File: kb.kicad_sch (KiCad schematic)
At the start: 191 parts, among them J1 Conn_02x04, J2 10029449-001RLF, J3 Conn_01x05, J4 Conn_01x10, J5 Conn_01x07, J6 Conn_01x06, SW1 RotaryEncoder_Switch, U1 Pico, U2 TXB0101DBVR

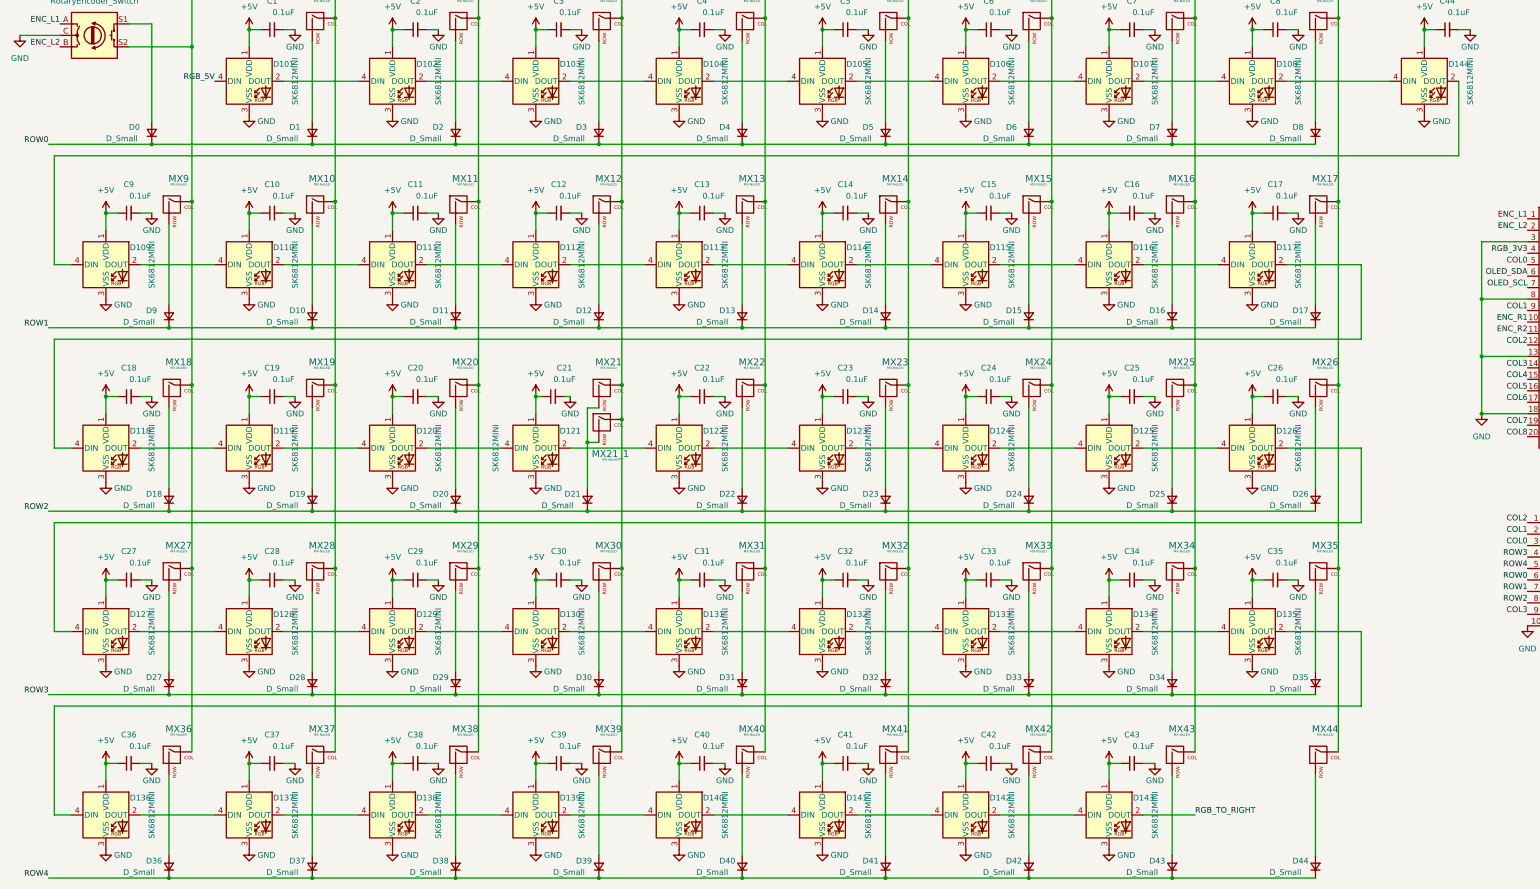
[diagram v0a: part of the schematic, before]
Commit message: start routing thru hole version
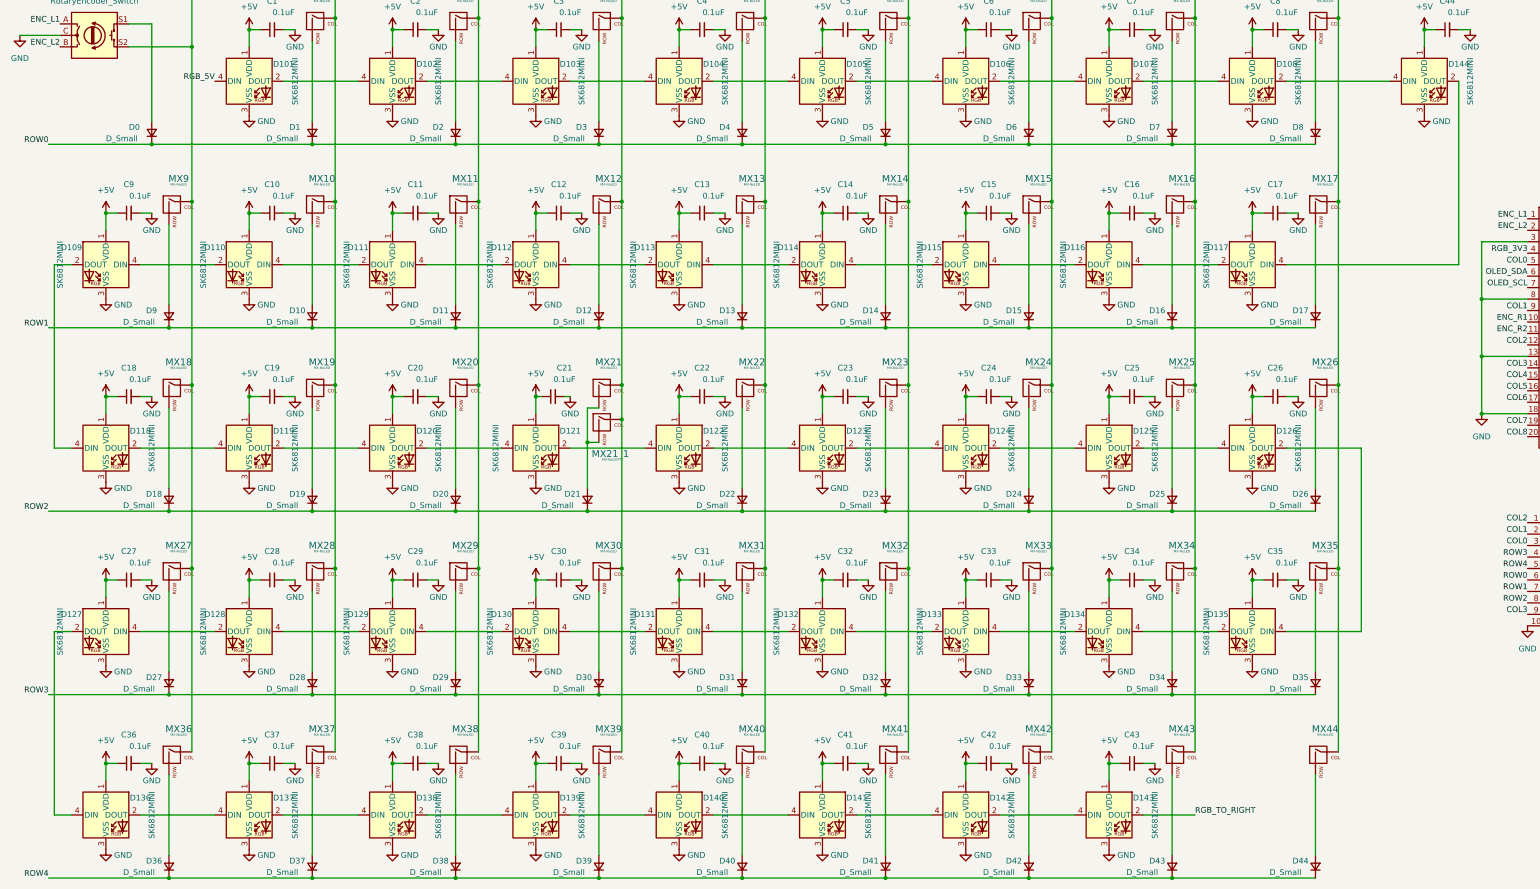
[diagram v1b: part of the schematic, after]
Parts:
- D0, D1, D10, D11, D12, D13, D14, D15, D16, D17, D18, D19, D2, D20, D21, D22, D23, D24, D25, D26, D27, D28, D29, D3, D30, D31, D32, D33, D34, D35, D36, D37, D38, D39, D4, D40, D41, D42, D43, D44, D5, D6, D7, D8, D9: footprint Diode_SMD:D_SOD-123 -> Keebio-Parts:Diode-Hybrid-Back
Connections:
- net at D144.2 (DOUT): now also D117.4 (DIN); no longer D109.4 (DIN)
- net at D135.2 (DOUT): now also D134.4 (DIN); no longer D136.4 (DIN)
- net at D135.4 (DIN): now also D126.2 (DOUT); no longer D134.2 (DOUT)
- net at D115.2 (DOUT): now also D114.4 (DIN); no longer D116.4 (DIN)
- net at D115.4 (DIN): now also D116.2 (DOUT); no longer D114.2 (DOUT)
- net at D112.2 (DOUT): now also D111.4 (DIN); no longer D113.4 (DIN)
- net at D112.4 (DIN): now also D113.2 (DOUT); no longer D111.2 (DOUT)
- net at D128.2 (DOUT): now also D127.4 (DIN); no longer D129.4 (DIN)
- net at D128.4 (DIN): now also D129.2 (DOUT); no longer D127.2 (DOUT)
- net at D130.4 (DIN): now also D131.2 (DOUT); no longer D129.2 (DOUT)
- net at D130.2 (DOUT): now also D129.4 (DIN); no longer D131.4 (DIN)
- net at D110.2 (DOUT): now also D109.4 (DIN); no longer D111.4 (DIN)
- net at D110.4 (DIN): now also D111.2 (DOUT); no longer D109.2 (DOUT)
- net at D133.2 (DOUT): now also D132.4 (DIN); no longer D134.4 (DIN)
- net at D133.4 (DIN): now also D134.2 (DOUT); no longer D132.2 (DOUT)
- net at D117.2 (DOUT): now also D116.4 (DIN); no longer D118.4 (DIN)
- new net: D127.2 (DOUT), D136.4 (DIN)
- new net: D113.4 (DIN), D114.2 (DOUT)
- new net: D131.4 (DIN), D132.2 (DOUT)
- new net: D109.2 (DOUT), D118.4 (DIN)

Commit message: all wired up??
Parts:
- removed J3: Conn_01x05, Connector_PinHeader_2.54mm:PinHeader_1x05_P2.54mm_Vertical, symbol Connector_Generic:Conn_01x05
- removed J4: Conn_01x10, Connector_PinHeader_2.54mm:PinHeader_1x10_P2.54mm_Vertical, symbol Connector_Generic:Conn_01x10
- removed J5: Conn_01x07, Connector_PinHeader_2.54mm:PinHeader_1x07_P2.54mm_Vertical, symbol Connector_Generic:Conn_01x07
- D0, D1, D10, D11, D18, D19, D2, D20, D27, D28, D29, D36, D37, D38, D9: footprint Keebio-Parts:Diode-Hybrid-Back -> Diode_SMD:D_SOD-123
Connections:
- net +5V: no longer J6.3 (Pin_3)
- net COL0: now also J2.9, U1.1 (GPIO0); no longer J2.6, U1.5 (GPIO3)
- net COL1: now also J2.8, U1.6 (GPIO4); no longer J2.7, U1.9 (GPIO6)
- net COL2: now also J2.7, U1.7 (GPIO5); no longer J2.8, U1.12 (GPIO9)
- net COL3: now also J2.6; no longer J2.9
- net COL4: now also J2.5; no longer J2.10
- net COL5: now also J2.4; no longer J2.11
- net COL6: now also J2.3; no longer J2.12
- net COL7: now also J2.2; no longer J2.13
- net COL8: now also J2.1; no longer J2.14
- net ENC_L1: now also U1.4 (GPIO2); no longer U1.1 (GPIO0)
- net ENC_R1: now also U1.21 (GPIO16); no longer U1.10 (GPIO7)
- net ENC_R2: now also U1.22 (GPIO17); no longer U1.11 (GPIO8)
- net GND: no longer J6.4 (Pin_4)
- net OLED_SCL: now also U1.32 (GPIO27_ADC1); no longer U1.7 (GPIO5)
- net OLED_SDA: now also U1.31 (GPIO26_ADC0); no longer U1.6 (GPIO4)
- net RGB_3V3: now also U1.5 (GPIO3); no longer U1.4 (GPIO2)
- net RGB_5V: now also J6.3 (Pin_3)
- net RGB_TO_RIGHT: now also J6.4 (Pin_4)
- net ROW1: now also U1.9 (GPIO6); no longer U1.32 (GPIO27_ADC1)
- net ROW2: now also U1.10 (GPIO7); no longer U1.31 (GPIO26_ADC0)
- net ROW3: now also U1.11 (GPIO8); no longer U1.29 (GPIO22)
- net ROW4: now also U1.12 (GPIO9); no longer U1.27 (GPIO21)
- net ROW5: now also J2.10, U1.29 (GPIO22); no longer J2.5, U1.26 (GPIO20)
- net ROW6: now also J2.11, U1.27 (GPIO21); no longer J2.4, U1.25 (GPIO19)
- net ROW7: now also J2.12, U1.26 (GPIO20); no longer J2.3, U1.24 (GPIO18)
- net ROW8: now also J2.13, U1.25 (GPIO19); no longer J2.2, U1.22 (GPIO17)
- net ROW9: now also J2.14, U1.24 (GPIO18); no longer J2.1, U1.21 (GPIO16)

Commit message: finished routing?45 deg hdmi
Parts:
- D12, D21, D3, D30, D39: footprint Keebio-Parts:Diode-Hybrid-Back -> Diode_SMD:D_SOD-123
- R1, R2: footprint Resistor_SMD:R_0805_2012Metric_Pad1.20x1.40mm_HandSolder -> Resistor_THT:R_Axial_DIN0207_L6.3mm_D2.5mm_P10.16mm_Horizontal
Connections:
- net +3V3: now also J1.3 (Pin_3); no longer J1.5 (Pin_5)
- net COL0: now also J2.1; no longer J2.9
- net COL1: now also J2.2; no longer J2.8
- net COL2: now also J2.3; no longer J2.7
- net COL3: now also J2.4; no longer J2.6
- net COL4: now also U1.20 (GPIO15); no longer U1.15 (GPIO11)
- net COL5: now also J2.6, U1.19 (GPIO14); no longer J2.4, U1.16 (GPIO12)
- net COL6: now also J2.7; no longer J2.3
- net COL7: now also J2.8, U1.16 (GPIO12); no longer J2.2, U1.19 (GPIO14)
- net COL8: now also J2.9, U1.15 (GPIO11); no longer J2.1, U1.20 (GPIO15)
- net ENC_R1: now also J2.11; no longer J2.16
- net ENC_R2: now also J2.10; no longer J2.15
- net GND: now also J1.1 (Pin_1); no longer J1.7 (Pin_7)
- net OLED_SCL: now also J1.5 (Pin_5); no longer J1.3 (Pin_3)
- net OLED_SDA: now also J1.7 (Pin_7); no longer J1.1 (Pin_1)
- net ROW5: now also J2.12; no longer J2.10
- net ROW6: now also J2.13; no longer J2.11
- net ROW7: now also J2.14; no longer J2.12
- net ROW8: now also J2.15; no longer J2.13
- net ROW9: now also J2.16; no longer J2.14

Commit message: finish routing 4x5 diodes
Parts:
- D13, D22, D31, D4, D40: footprint Keebio-Parts:Diode-Hybrid-Back -> Diode_SMD:D_SOD-123
- J1: footprint Connector_PinHeader_2.54mm:PinHeader_2x04_P2.54mm_Vertical -> Connector_PinSocket_2.54mm:PinSocket_2x04_P2.54mm_Vertical
- J6: footprint Connector_PinHeader_2.54mm:PinHeader_1x06_P2.54mm_Vertical -> Connector_PinSocket_2.54mm:PinSocket_1x06_P2.54mm_Vertical
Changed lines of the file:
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@@
       (effects (font (size 1.27 1.27)) (justify right))
     )
-    (property "Footprint" "Keebio-Parts:Diode-Hybrid-Back" (id 2) (at 179.07 186.69 90)
+    (property "Footprint" "Diode_SMD:D_SOD-123" (id 2) (at 179.07 186.69 90)
       (effects (font (size 1.27 1.27)) hide)
     )
@@
     (property "Reference" "J1" (id 0) (at 243.84 22.86 0))
     (property "Value" "Conn_02x04" (id 1) (at 247.65 25.4 0))
-    (property "Footprint" "Connector_PinHeader_2.54mm:PinHeader_2x04_P2.54mm_Vertical" (id 2) (at 242.57 31.75 0)
+    (property "Footprint" "Connector_PinSocket_2.54mm:PinSocket_2x04_P2.54mm_Vertical" (id 2) (at 242.57 31.75 0)
       (effects (font (size 1.27 1.27)) hide)
     )
@@
       (effects (font (size 1.27 1.27)) (justify right))
     )
-    (property "Footprint" "Keebio-Parts:Diode-Hybrid-Back" (id 2) (at 179.07 267.97 90)
+    (property "Footprint" "Diode_SMD:D_SOD-123" (id 2) (at 179.07 267.97 90)
       (effects (font (size 1.27 1.27)) hide)
     )
@@
       (effects (font (size 1.27 1.27)) (justify right))
     )
-    (property "Footprint" "Keebio-Parts:Diode-Hybrid-Back" (id 2) (at 179.07 146.05 90)
+    (property "Footprint" "Diode_SMD:D_SOD-123" (id 2) (at 179.07 146.05 90)
       (effects (font (size 1.27 1.27)) hide)
     )
@@
       (effects (font (size 1.27 1.27)) (justify right))
     )
-    (property "Footprint" "Keebio-Parts:Diode-Hybrid-Back" (id 2) (at 179.07 227.33 90)
+    (property "Footprint" "Diode_SMD:D_SOD-123" (id 2) (at 179.07 227.33 90)
       (effects (font (size 1.27 1.27)) hide)
     )
@@
       (effects (font (size 1.27 1.27)) (justify left))
     )
-    (property "Footprint" "Connector_PinHeader_2.54mm:PinHeader_1x06_P2.54mm_Vertical" (id 2) (at 393.7 226.06 0)
+    (property "Footprint" "Connector_PinSocket_2.54mm:PinSocket_1x06_P2.54mm_Vertical" (id 2) (at 393.7 226.06 0)
       (effects (font (size 1.27 1.27)) hide)
     )
@@
       (effects (font (size 1.27 1.27)) (justify right))
     )
-    (property "Footprint" "Keebio-Parts:Diode-Hybrid-Back" (id 2) (at 179.07 105.41 90)
+    (property "Footprint" "Diode_SMD:D_SOD-123" (id 2) (at 179.07 105.41 90)
       (effects (font (size 1.27 1.27)) hide)
     )
@@
     )
     (path "/da8be1c2-ae61-4d13-8788-f80187bd54cf"
-      (reference "D4") (unit 1) (value "D_Small") (footprint "Keebio-Parts:Diode-Hybrid-Back")
+      (reference "D4") (unit 1) (value "D_Small") (footprint "Diode_SMD:D_SOD-123")
     )
     (path "/aa7826d1-0a77-42bf-ada8-10ee51561d22"
@@
     )
     (path "/496220a6-e54e-4b7c-af88-503b2971e62d"
-      (reference "D13") (unit 1) (value "D_Small") (footprint "Keebio-Parts:Diode-Hybrid-Back")
+      (reference "D13") (unit 1) (value "D_Small") (footprint "Diode_SMD:D_SOD-123")
     )
     (path "/1428aeb1-a1be-4bfd-8e86-f6aac5bb24b0"
@@
     )
     (path "/00f13922-4f95-4450-87ba-7ef0dab7ba88"
-      (reference "D22") (unit 1) (value "D_Small") (footprint "Keebio-Parts:Diode-Hybrid-Back")
+      (reference "D22") (unit 1) (value "D_Small") (footprint "Diode_SMD:D_SOD-123")
     )
     (path "/9b42d764-8fe1-4fb3-a88d-f5fdea18ad57"
@@
     )
     (path "/7d59c8b1-ccc0-48b5-9829-a91e9bbb6fc6"
-      (reference "D31") (unit 1) (value "D_Small") (footprint "Keebio-Parts:Diode-Hybrid-Back")
+      (reference "D31") (unit 1) (value "D_Small") (footprint "Diode_SMD:D_SOD-123")
     )
     (path "/404863d6-1ddc-4a88-9b20-ef96aa16758f"
@@
     )
     (path "/472fa51d-88ac-48c3-ae52-a761d5c3cf9a"
-      (reference "D40") (unit 1) (value "D_Small") (footprint "Keebio-Parts:Diode-Hybrid-Back")
+      (reference "D40") (unit 1) (value "D_Small") (footprint "Diode_SMD:D_SOD-123")
     )
     (path "/6886faaf-5191-4c14-821f-b0b6efaecbc7"
@@
     )
     (path "/0b55160c-0a06-413f-a5da-1c6d6b7157c7"
-      (reference "J1") (unit 1) (value "Conn_02x04") (footprint "Connector_PinHeader_2.54mm:PinHeader_2x04_P2.54mm_Vertical")
+      (reference "J1") (unit 1) (value "Conn_02x04") (footprint "Connector_PinSocket_2.54mm:PinSocket_2x04_P2.54mm_Vertical")
     )
     (path "/6bd8bd76-8614-429d-a556-5fcda9f7b2c7"
@@
     )
     (path "/a252f866-89e7-4b0c-a051-b3d9be2a2683"
-      (reference "J6") (unit 1) (value "Conn_01x06") (footprint "Connector_PinHeader_2.54mm:PinHeader_1x06_P2.54mm_Vertical")
+      (reference "J6") (unit 1) (value "Conn_01x06") (footprint "Connector_PinSocket_2.54mm:PinSocket_1x06_P2.54mm_Vertical")
     )
     (path "/8a089bf5-08f1-41ee-aa36-391f5cdf0f9d"

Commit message: sch, pcb checked
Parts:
- renumbered J6 to J3
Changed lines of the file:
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@@
   (symbol (lib_id "Connector_Generic:Conn_01x06") (at 393.7 226.06 0) (unit 1)
     (in_bom yes) (on_board yes)
-    (property "Reference" "J6" (id 0) (at 396.24 226.06 0)
+    (property "Reference" "J3" (id 0) (at 396.24 226.06 0)
       (effects (font (size 1.27 1.27)) (justify left))
     )
@@
     )
     (path "/a252f866-89e7-4b0c-a051-b3d9be2a2683"
-      (reference "J6") (unit 1) (value "Conn_01x06") (footprint "Connector_PinSocket_2.54mm:PinSocket_1x06_P2.54mm_Vertical")
+      (reference "J3") (unit 1) (value "Conn_01x06") (footprint "Connector_PinSocket_2.54mm:PinSocket_1x06_P2.54mm_Vertical")
     )
     (path "/8a089bf5-08f1-41ee-aa36-391f5cdf0f9d"

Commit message: add sideways encoder support
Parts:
- added C47, C48: 10nF, Capacitor_SMD:C_0805_2012Metric_Pad1.18x1.45mm_HandSolder, symbol Device:C_Small
- added R3, R4, R5, R6: 10k, Resistor_SMD:R_0805_2012Metric_Pad1.20x1.40mm_HandSolder, symbol Device:R_Small_US
- added SW2: RotaryEncoder, Keebio-Parts:RotaryEncoder_EC11B-Horizontal-No-Pushbutton, symbol Device:RotaryEncoder
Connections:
- net +3V3: now also R3.1, R4.1
- net COL0: now also SW1.S1, U1.4 (GPIO2); no longer SW1.S2, U1.1 (GPIO0)
- net ENC_L1: now also R3.2, R5.2, SW2.A; no longer U1.4 (GPIO2)
- net ENC_L2: now also R4.2, R6.1, SW2.B; no longer U1.2 (GPIO1)
- net GND: now also C47.2, C48.2, SW2.C
- net at D0.2 (A): now also SW1.S2; no longer SW1.S1
- new net ENC_L1_CLEAN: C47.1, R5.1, U1.2 (GPIO1)
- new net ENC_L2_CLEAN: C48.1, R6.2, U1.1 (GPIO0)
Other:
- moved on the sheet: C45, C46, D0, U2

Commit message: Add right encoder filtering
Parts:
- added C49, C50: 10nF, Capacitor_SMD:C_0805_2012Metric_Pad1.18x1.45mm_HandSolder, symbol Device:C_Small
- added R10, R7, R8, R9: 10k, Resistor_SMD:R_0805_2012Metric_Pad1.20x1.40mm_HandSolder, symbol Device:R_Small_US
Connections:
- net +3V3: now also R7.1, R8.1
- net ENC_R1: now also R7.2, R9.2; no longer U1.21 (GPIO16)
- net ENC_R2: now also R10.1, R8.2; no longer U1.22 (GPIO17)
- net GND: now also C49.2, C50.2
- new net ENC_R1_CLEAN: C49.1, R9.1, U1.21 (GPIO16)
- new net ENC_R2_CLEAN: C50.1, R10.2, U1.22 (GPIO17)
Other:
- moved on the sheet: C45, C46, C47, C48, J1, R1, R2, R3, R4, R5, R6, U2

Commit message: reroute enc filter
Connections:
- net ENC_R1_CLEAN: now also U1.27 (GPIO21); no longer U1.21 (GPIO16)
- net ENC_R2_CLEAN: now also U1.29 (GPIO22); no longer U1.22 (GPIO17)
- net ROW5: now also U1.26 (GPIO20); no longer U1.29 (GPIO22)
- net ROW6: now also U1.25 (GPIO19); no longer U1.27 (GPIO21)
- net ROW7: now also U1.24 (GPIO18); no longer U1.26 (GPIO20)
- net ROW8: now also U1.22 (GPIO17); no longer U1.25 (GPIO19)
- net ROW9: now also U1.21 (GPIO16); no longer U1.24 (GPIO18)
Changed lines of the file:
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@@
     (effects (font (size 1.27 1.27)) (justify right bottom))
+  )
+  (label "ROW6" (at 388.62 162.56 0)
+    (effects (font (size 1.27 1.27)) (justify left bottom))
   )
   (label "COL6" (at 247.65 67.31 90)
     (effects (font (size 1.27 1.27)) (justify left bottom))
   )
+  (label "ROW5" (at 388.62 160.02 0)
+    (effects (font (size 1.27 1.27)) (justify left bottom))
+  )
   (label "RGB_5V" (at 388.62 226.06 180)
     (effects (font (size 1.27 1.27)) (justify right bottom))
@@
     (effects (font (size 1.27 1.27)) (justify right bottom))
   )
-  (label "ROW7" (at 388.62 160.02 0)
-    (effects (font (size 1.27 1.27)) (justify left bottom))
-  )
   (label "ENC_R2" (at 199.39 31.75 180)
     (effects (font (size 1.27 1.27)) (justify right bottom))
   )
+  (label "ROW8" (at 388.62 170.18 0)
+    (effects (font (size 1.27 1.27)) (justify left bottom))
+  )
   (label "COL4" (at 184.15 67.31 90)
     (effects (font (size 1.27 1.27)) (justify left bottom))
   )
-  (label "ENC_R1_CLEAN" (at 388.62 172.72 0)
-    (effects (font (size 1.27 1.27)) (justify left bottom))
-  )
   (label "COL5" (at 353.06 170.18 180)
     (effects (font (size 1.27 1.27)) (justify right bottom))
@@
     (effects (font (size 1.27 1.27)) (justify right bottom))
   )
+  (label "ROW9" (at 388.62 172.72 0)
+    (effects (font (size 1.27 1.27)) (justify left bottom))
+  )
   (label "COL2" (at 353.06 139.7 180)
     (effects (font (size 1.27 1.27)) (justify right bottom))
@@
     (effects (font (size 1.27 1.27)) (justify right bottom))
   )
-  (label "ROW6" (at 388.62 157.48 0)
-    (effects (font (size 1.27 1.27)) (justify left bottom))
-  )
   (label "COL3" (at 152.4 67.31 90)
     (effects (font (size 1.27 1.27)) (justify left bottom))
@@
     (effects (font (size 1.27 1.27)) (justify right bottom))
   )
-  (label "ROW8" (at 388.62 162.56 0)
-    (effects (font (size 1.27 1.27)) (justify left bottom))
-  )
   (label "COL0" (at 353.06 132.08 180)
     (effects (font (size 1.27 1.27)) (justify right bottom))
@@
     (effects (font (size 1.27 1.27)) (justify left bottom))
   )
-  (label "ROW9" (at 388.62 165.1 0)
+  (label "ENC_R2_CLEAN" (at 388.62 152.4 0)
     (effects (font (size 1.27 1.27)) (justify left bottom))
   )
@@
     (effects (font (size 1.27 1.27)) (justify left bottom))
   )
+  (label "ROW7" (at 388.62 165.1 0)
+    (effects (font (size 1.27 1.27)) (justify left bottom))
+  )
   (label "ROW2" (at 353.06 147.32 180)
     (effects (font (size 1.27 1.27)) (justify right bottom))
@@
     (effects (font (size 1.27 1.27)) (justify right bottom))
   )
-  (label "ROW5" (at 388.62 152.4 0)
-    (effects (font (size 1.27 1.27)) (justify left bottom))
-  )
   (label "COL5" (at 381 30.48 0)
     (effects (font (size 1.27 1.27)) (justify left bottom))
@@
     (effects (font (size 1.27 1.27)) (justify right bottom))
   )
-  (label "ENC_R2_CLEAN" (at 388.62 170.18 0)
-    (effects (font (size 1.27 1.27)) (justify left bottom))
-  )
   (label "OLED_SDA" (at 297.18 29.21 0)
     (effects (font (size 1.27 1.27)) (justify left bottom))
@@
     (effects (font (size 1.27 1.27)) (justify right bottom))
   )
+  (label "ENC_R1_CLEAN" (at 388.62 157.48 0)
+    (effects (font (size 1.27 1.27)) (justify left bottom))
+  )
   (label "RGB_3V3" (at 353.06 134.62 180)
